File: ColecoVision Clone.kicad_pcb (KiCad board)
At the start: 2 copper layers, 149.4 x 99.1 mm, 141 parts, among them J1 Cartridge Slot, J2 Composite video, J3 PJ-102A, J4 RCJ-017, J5 Controller Port 1, J6 Controller Port 2, Q1 2n4401, Q2 Q_NJFET_DGS, Q3 2N3904, Q4 2N3904, Q5 2N3904, SW1 Power Toggle, SW2 Reset, U1 Z80CPU, U10 SN76489AN, U12 74LS138 (Mem. Mapped), U13 74LS138 (I/O), U14 74LS02, U15 Controller 1, U16 Controller 2, U17 74LS05, U18 74LS05, U19 74HC04, U2 Work RAM, U20 74LS74, U21 74HC04, U22 74LS74, U23 74HCT00, U24 TPS60403DBVR, U3 BIOS ROM 27C256, U4 74HCT04, U5 TMS9918A, U6 74LS574, U7 74LS574, U8 74LS574, U9 VRAM, X1 14.31818MHz

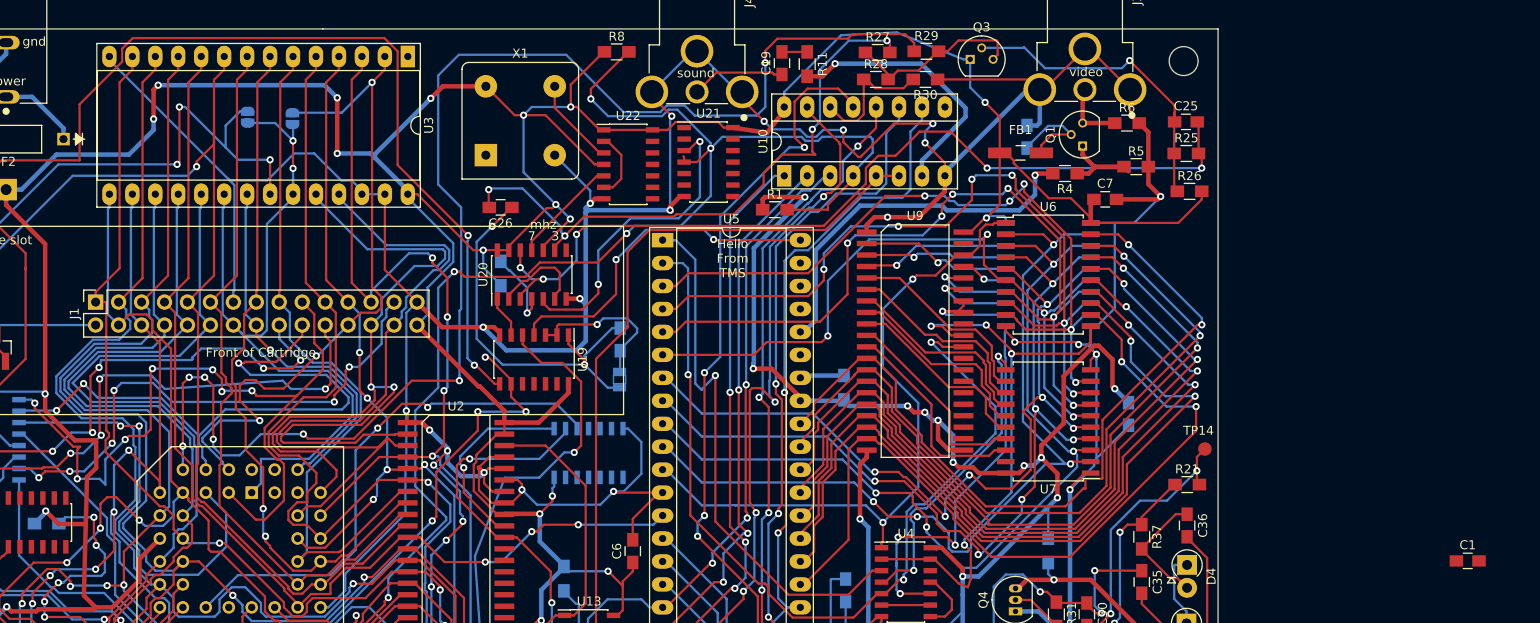
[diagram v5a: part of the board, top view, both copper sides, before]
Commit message: BIOS ROM decouple
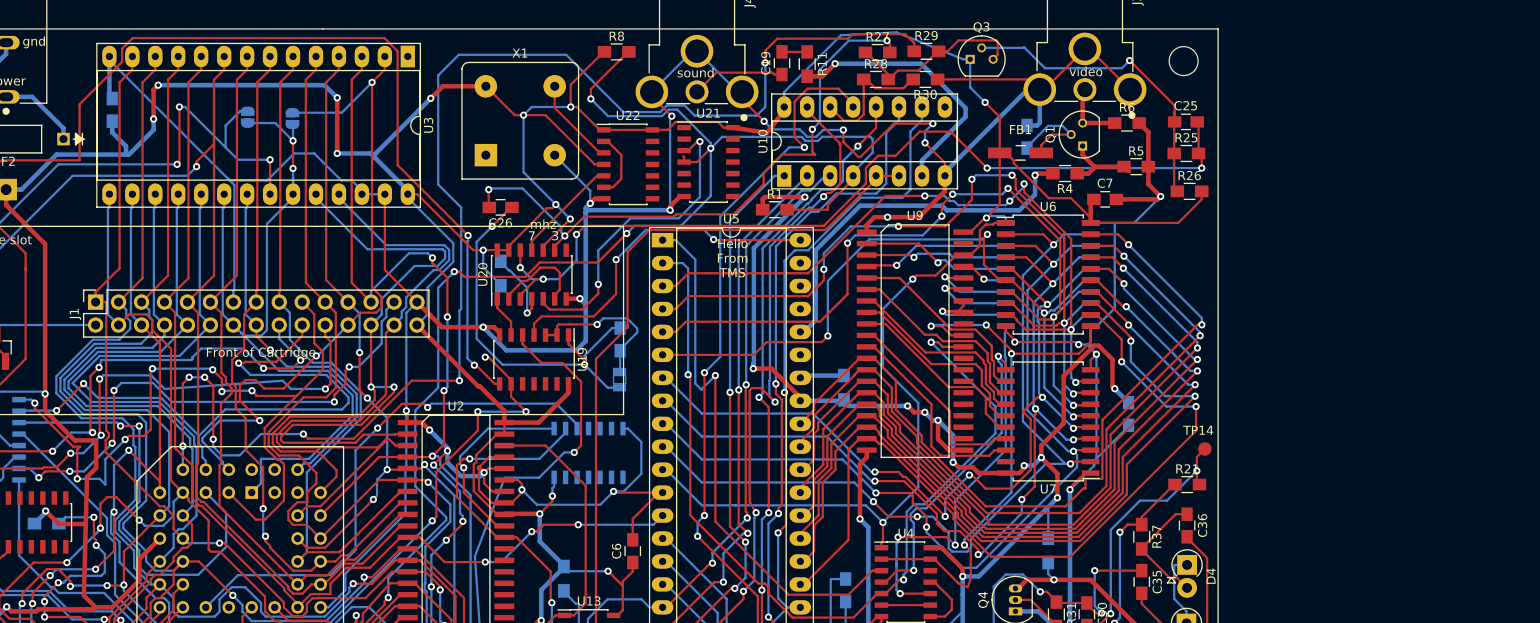
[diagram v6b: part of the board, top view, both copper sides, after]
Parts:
- C1: moved to B.Cu
- moved C1 158.1 mm to (-48.7, 36.9), turned to 90 degrees
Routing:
- net GND: track 871.5 -> 876.3 mm
- net VCC: track 839.4 -> 843.8 mm
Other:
- board text added: ""grime pilot""
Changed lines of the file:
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@@
   (general
     (thickness 1.6)
-    (drawings 27)
-    (tracks 4469)
+    (drawings 28)
+    (tracks 4475)
     (zones 0)
     (modules 141)
@@
     )
   )
-  (module Capacitors_SMD:C_0805_HandSoldering (layer F.Cu)
-    (at 101.2825 86.8045)
+  (module Capacitors_SMD:C_0805_HandSoldering (layer B.Cu)
+    (at -48.7045 36.8935 90)
     (descr "Capacitor SMD 0805, hand soldering")
     (tags "capacitor 0805")
     (attr smd)
-    (fp_text reference C1 (at 0 -1.75) (layer F.SilkS)
-      (effects (font (size 1 1) (thickness 0.15)))
+    (fp_text reference C1 (at 0 1.75 -90) (layer B.SilkS)
+      (effects (font (size 1 1) (thickness 0.15)) (justify mirror))
     )
-    (fp_text value 0.1µF (at 0 1.75) (layer F.Fab)
-      (effects (font (size 1 1) (thickness 0.15)))
+    (fp_text value 0.1µF (at 0 -1.75 -90) (layer B.Fab)
+      (effects (font (size 1 1) (thickness 0.15)) (justify mirror))
     )
-    (fp_text user %R (at 0 -1.75) (layer F.Fab)
-      (effects (font (size 1 1) (thickness 0.15)))
+    (fp_text user %R (at 0 1.75 -90) (layer B.Fab)
+      (effects (font (size 1 1) (thickness 0.15)) (justify mirror))
     )
-    (fp_line (start -1 0.62) (end -1 -0.62) (layer F.Fab) (width 0.1))
-    (fp_line (start 1 0.62) (end -1 0.62) (layer F.Fab) (width 0.1))
-    (fp_line (start 1 -0.62) (end 1 0.62) (layer F.Fab) (width 0.1))
-    (fp_line (start -1 -0.62) (end 1 -0.62) (layer F.Fab) (width 0.1))
-    (fp_line (start 0.5 -0.85) (end -0.5 -0.85) (layer F.SilkS) (width 0.12))
-    (fp_line (start -0.5 0.85) (end 0.5 0.85) (layer F.SilkS) (width 0.12))
-    (fp_line (start -2.25 -0.88) (end 2.25 -0.88) (layer F.CrtYd) (width 0.05))
-    (fp_line (start -2.25 -0.88) (end -2.25 0.87) (layer F.CrtYd) (width 0.05))
-    (fp_line (start 2.25 0.87) (end 2.25 -0.88) (layer F.CrtYd) (width 0.05))
-    (fp_line (start 2.25 0.87) (end -2.25 0.87) (layer F.CrtYd) (width 0.05))
-    (pad 1 smd rect (at -1.25 0) (size 1.5 1.25) (layers F.Cu F.Paste F.Mask)
+    (fp_line (start -1 -0.62) (end -1 0.62) (layer B.Fab) (width 0.1))
+    (fp_line (start 1 -0.62) (end -1 -0.62) (layer B.Fab) (width 0.1))
+    (fp_line (start 1 0.62) (end 1 -0.62) (layer B.Fab) (width 0.1))
+    (fp_line (start -1 0.62) (end 1 0.62) (layer B.Fab) (width 0.1))
+    (fp_line (start 0.5 0.85) (end -0.5 0.85) (layer B.SilkS) (width 0.12))
+    (fp_line (start -0.5 -0.85) (end 0.5 -0.85) (layer B.SilkS) (width 0.12))
+    (fp_line (start -2.25 0.88) (end 2.25 0.88) (layer B.CrtYd) (width 0.05))
+    (fp_line (start -2.25 0.88) (end -2.25 -0.87) (layer B.CrtYd) (width 0.05))
+    (fp_line (start 2.25 -0.87) (end 2.25 0.88) (layer B.CrtYd) (width 0.05))
+    (fp_line (start 2.25 -0.87) (end -2.25 -0.87) (layer B.CrtYd) (width 0.05))
+    (pad 1 smd rect (at -1.25 0 90) (size 1.5 1.25) (layers B.Cu B.Paste B.Mask)
       (net 19 VCC))
-    (pad 2 smd rect (at 1.25 0) (size 1.5 1.25) (layers F.Cu F.Paste F.Mask)
+    (pad 2 smd rect (at 1.25 0 90) (size 1.5 1.25) (layers B.Cu B.Paste B.Mask)
       (net 10 GND))
     (model Capacitors_SMD.3dshapes/C_0805.wrl
@@
       (xy -3.70249 -1.164682) (xy -3.429 -1.183342) (xy -2.925182 -1.118187)) (layer F.SilkS) (width 0.01))
   )
+  (gr_text "\"grime pilot\"" (at -62.5475 124.968) (layer B.SilkS)
+    (effects (font (size 1 1) (thickness 0.15)) (justify mirror))
+  )
   (gr_text power (at -60.3885 33.7185) (layer F.SilkS)
     (effects (font (size 1 1) (thickness 0.15)))
@@
   (segment (start 66.9925 46.7995) (end 67.31 46.482) (width 0.5) (layer F.Cu) (net 10))
   (segment (start 62.4205 46.7995) (end 66.9925 46.7995) (width 0.5) (layer F.Cu) (net 10))
+  (segment (start -49.022 35.326) (end -48.7045 35.6435) (width 0.5) (layer B.Cu) (net 10))
+  (segment (start -49.022 30.988) (end -49.022 35.326) (width 0.5) (layer B.Cu) (net 10))
   (segment (start 7.214 92.837) (end 7.7855 92.2655) (width 0.25) (layer F.Cu) (net 19) (status 10))
   (segment (start 6.764 92.837) (end 7.214 92.837) (width 0.25) (layer F.Cu) (net 19) (status 30))
@@
   (segment (start -58.752 45.72) (end -54.8785 41.8465) (width 0.5) (layer B.Cu) (net 19))
   (segment (start -60.452 45.72) (end -58.752 45.72) (width 0.5) (layer B.Cu) (net 19) (status 10))
-  (segment (start -54.8785 41.8465) (end -46.863 41.8465) (width 0.5) (layer B.Cu) (net 19))
   (segment (start -46.863 41.8465) (end -44.1325 39.116) (width 0.5) (layer B.Cu) (net 19))
   (segment (start -44.1325 39.116) (end -44.1325 37.9095) (width 0.5) (layer B.Cu) (net 19))
@@
   (segment (start 59.564 47.156) (end 59.9205 46.7995) (width 0.5) (layer F.Cu) (net 19))
   (segment (start 59.564 49.403) (end 59.564 47.156) (width 0.5) (layer F.Cu) (net 19))
+  (segment (start -48.7045 39.3935) (end -47.1805 40.9175) (width 0.5) (layer B.Cu) (net 19))
+  (segment (start -48.7045 38.1435) (end -48.7045 39.3935) (width 0.5) (layer B.Cu) (net 19))
+  (segment (start -47.1805 41.8465) (end -46.863 41.8465) (width 0.5) (layer B.Cu) (net 19))
+  (segment (start -47.1805 40.9175) (end -47.1805 41.8465) (width 0.5) (layer B.Cu) (net 19))
+  (segment (start -54.8785 41.8465) (end -47.1805 41.8465) (width 0.5) (layer B.Cu) (net 19))
   (via (at 53.407809 44.12749) (size 0.8) (drill 0.4) (layers F.Cu B.Cu) (net 20))
   (segment (start 53.407809 46.274879) (end 53.407809 44.693175) (width 0.5) (layer B.Cu) (net 20))

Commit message: SO CLOSE
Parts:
- C10, C11, C14, C16, C18, C29: moved to B.Cu
- moved C17 321.2 mm to (-64.3, 75.7), turned to 270 degrees
- moved C15 283.2 mm to (-52.2, 52.4), turned to 90 degrees
- moved C18 272.9 mm to (-32.7, 86.6)
- moved C14 261.9 mm to (-10.3, 72.0), turned to 270 degrees
- moved C2 254.4 mm to (-11.3, 38.4), turned to 270 degrees
- moved C16 252.7 mm to (4.00, 85.2)
- moved C29 243.9 mm to (-3.22, 39.9)
- moved C9 100.9 mm to (67.5, 54.8), turned to 270 degrees
- moved C11 90.9 mm to (39.9, 73.7), turned to 180 degrees
- moved C10 90.4 mm to (40.4, 65.6)
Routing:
- net GND: track 876.3 -> 1006.4 mm, vias 48 -> 57
- net VCC: track 843.8 -> 906.4 mm, vias 43 -> 46
- net A4: track 79.7 -> 84.7 mm
- net RW: track 75.1 -> 78.1 mm
- net D7: track 296.9 -> 299.3 mm
- net VD6: track 86.6 -> 85.2 mm
- net AD7: track 82.7 -> 83.8 mm
- net D3: track 268.0 -> 267.4 mm

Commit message: 3
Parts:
- C28: moved to B.Cu
- moved C28 236.2 mm to (8.51, 43.1), turned to 270 degrees
- moved C13 227.1 mm to (46.4, 37.2), turned to 270 degrees
- moved C22 183.6 mm to (50.9, 97.0)
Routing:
- net GND: track 1006.4 -> 1021.3 mm
- net VCC: track 906.4 -> 915.8 mm, vias 46 -> 47
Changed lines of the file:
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@@
     (thickness 1.6)
     (drawings 28)
-    (tracks 4619)
+    (tracks 4632)
     (zones 0)
     (modules 141)
@@
     )
   )
-  (module Capacitors_SMD:C_0805_HandSoldering (layer F.Cu)
-    (at 223.608 140.692)
+  (module Capacitors_SMD:C_0805_HandSoldering (layer B.Cu)
+    (at 8.509 43.053 270)
     (descr "Capacitor SMD 0805, hand soldering")
     (tags "capacitor 0805")
     (attr smd)
-    (fp_text reference C28 (at 0 -1.75) (layer F.SilkS)
-      (effects (font (size 1 1) (thickness 0.15)))
+    (fp_text reference C28 (at 0 1.75 270) (layer B.SilkS)
+      (effects (font (size 1 1) (thickness 0.15)) (justify mirror))
     )
-    (fp_text value 0.1µF (at 0 1.75) (layer F.Fab)
-      (effects (font (size 1 1) (thickness 0.15)))
+    (fp_text value 0.1µF (at 0 -1.75 270) (layer B.Fab)
+      (effects (font (size 1 1) (thickness 0.15)) (justify mirror))
     )
-    (fp_text user %R (at 0 -1.75) (layer F.Fab)
-      (effects (font (size 1 1) (thickness 0.15)))
+    (fp_text user %R (at 0 1.75 270) (layer B.Fab)
+      (effects (font (size 1 1) (thickness 0.15)) (justify mirror))
     )
-    (fp_line (start -1 0.62) (end -1 -0.62) (layer F.Fab) (width 0.1))
-    (fp_line (start 1 0.62) (end -1 0.62) (layer F.Fab) (width 0.1))
-    (fp_line (start 1 -0.62) (end 1 0.62) (layer F.Fab) (width 0.1))
-    (fp_line (start -1 -0.62) (end 1 -0.62) (layer F.Fab) (width 0.1))
-    (fp_line (start 0.5 -0.85) (end -0.5 -0.85) (layer F.SilkS) (width 0.12))
-    (fp_line (start -0.5 0.85) (end 0.5 0.85) (layer F.SilkS) (width 0.12))
-    (fp_line (start -2.25 -0.88) (end 2.25 -0.88) (layer F.CrtYd) (width 0.05))
-    (fp_line (start -2.25 -0.88) (end -2.25 0.87) (layer F.CrtYd) (width 0.05))
-    (fp_line (start 2.25 0.87) (end 2.25 -0.88) (layer F.CrtYd) (width 0.05))
-    (fp_line (start 2.25 0.87) (end -2.25 0.87) (layer F.CrtYd) (width 0.05))
-    (pad 1 smd rect (at -1.25 0) (size 1.5 1.25) (layers F.Cu F.Paste F.Mask)
+    (fp_line (start -1 -0.62) (end -1 0.62) (layer B.Fab) (width 0.1))
+    (fp_line (start 1 -0.62) (end -1 -0.62) (layer B.Fab) (width 0.1))
+    (fp_line (start 1 0.62) (end 1 -0.62) (layer B.Fab) (width 0.1))
+    (fp_line (start -1 0.62) (end 1 0.62) (layer B.Fab) (width 0.1))
+    (fp_line (start 0.5 0.85) (end -0.5 0.85) (layer B.SilkS) (width 0.12))
+    (fp_line (start -0.5 -0.85) (end 0.5 -0.85) (layer B.SilkS) (width 0.12))
+    (fp_line (start -2.25 0.88) (end 2.25 0.88) (layer B.CrtYd) (width 0.05))
+    (fp_line (start -2.25 0.88) (end -2.25 -0.87) (layer B.CrtYd) (width 0.05))
+    (fp_line (start 2.25 -0.87) (end 2.25 0.88) (layer B.CrtYd) (width 0.05))
+    (fp_line (start 2.25 -0.87) (end -2.25 -0.87) (layer B.CrtYd) (width 0.05))
+    (pad 1 smd rect (at -1.25 0 270) (size 1.5 1.25) (layers B.Cu B.Paste B.Mask)
       (net 19 VCC))
-    (pad 2 smd rect (at 1.25 0) (size 1.5 1.25) (layers F.Cu F.Paste F.Mask)
+    (pad 2 smd rect (at 1.25 0 270) (size 1.5 1.25) (layers B.Cu B.Paste B.Mask)
       (net 10 GND))
     (model Capacitors_SMD.3dshapes/C_0805.wrl
@@
   )
   (module Capacitors_SMD:C_0805_HandSoldering (layer F.Cu)
-    (at 228.548 143.512)
+    (at 50.947 96.9645)
     (descr "Capacitor SMD 0805, hand soldering")
     (tags "capacitor 0805")
@@
   )
   (module Capacitors_SMD:C_0805_HandSoldering (layer F.Cu)
-    (at 253.988 129.272)
+    (at 46.4185 37.1675 270)
     (descr "Capacitor SMD 0805, hand soldering")
     (tags "capacitor 0805")
     (attr smd)
-    (fp_text reference C13 (at 0 -1.75) (layer F.SilkS)
+    (fp_text reference C13 (at 0 -1.75 90) (layer F.SilkS)
       (effects (font (size 1 1) (thickness 0.15)))
     )
-    (fp_text value 0.1µF (at 0 1.75) (layer F.Fab)
+    (fp_text value 0.1µF (at 0 1.75 90) (layer F.Fab)
       (effects (font (size 1 1) (thickness 0.15)))
     )
-    (fp_text user %R (at 0 -1.75) (layer F.Fab)
+    (fp_text user %R (at 0 -1.75 90) (layer F.Fab)
       (effects (font (size 1 1) (thickness 0.15)))
     )
@@
     (fp_line (start 2.25 0.87) (end 2.25 -0.88) (layer F.CrtYd) (width 0.05))
     (fp_line (start 2.25 0.87) (end -2.25 0.87) (layer F.CrtYd) (width 0.05))
-    (pad 1 smd rect (at -1.25 0) (size 1.5 1.25) (layers F.Cu F.Paste F.Mask)
+    (pad 1 smd rect (at -1.25 0 270) (size 1.5 1.25) (layers F.Cu F.Paste F.Mask)
       (net 19 VCC))
-    (pad 2 smd rect (at 1.25 0) (size 1.5 1.25) (layers F.Cu F.Paste F.Mask)
+    (pad 2 smd rect (at 1.25 0 270) (size 1.5 1.25) (layers F.Cu F.Paste F.Mask)
       (net 10 GND))
     (model Capacitors_SMD.3dshapes/C_0805.wrl
@@
   (segment (start 1.981 48.971) (end 2.032 48.92) (width 0.25) (layer F.Cu) (net 19))
   (via (at 1.981 48.971) (size 0.8) (drill 0.4) (layers F.Cu B.Cu) (net 19))
-  (segment (start 4.682 42.926) (end -0.762 37.482) (width 0.25) (layer F.Cu) (net 19))
+  (segment (start 4.682 42.926) (end 3.9285 42.1725) (width 0.25) (layer F.Cu) (net 19))
   (segment (start 5.682 42.926) (end 4.682 42.926) (width 0.25) (layer F.Cu) (net 19) (status 10))
   (segment (start -4.174 37.482) (end -7.366 34.29) (width 0.25) (layer F.Cu) (net 19) (status 20))
@@
   (segment (start -32.893 85.217) (end -31.496 86.614) (width 0.5) (layer B.Cu) (net 10))
   (segment (start -32.893 83.312) (end -32.893 85.217) (width 0.5) (layer B.Cu) (net 10))
+  (segment (start 46.4185 38.4175) (end 42.1005 38.4175) (width 0.5) (layer F.Cu) (net 10))
+  (segment (start 52.197 93.345) (end 51.2445 92.3925) (width 0.5) (layer F.Cu) (net 10))
+  (segment (start 52.197 96.9645) (end 52.197 93.345) (width 0.5) (layer F.Cu) (net 10))
+  (segment (start 7.132 44.303) (end 4.191 47.244) (width 0.5) (layer B.Cu) (net 10))
+  (segment (start 8.509 44.303) (end 7.132 44.303) (width 0.5) (layer B.Cu) (net 10))
   (segment (start 7.214 92.837) (end 7.7855 92.2655) (width 0.25) (layer F.Cu) (net 19) (status 10))
   (segment (start 6.764 92.837) (end 7.214 92.837) (width 0.25) (layer F.Cu) (net 19) (status 30))
@@
   (segment (start -42.550501 85.211499) (end -43.434 84.328) (width 0.5) (layer B.Cu) (net 19))
   (segment (start -42.550501 85.719499) (end -42.550501 85.211499) (width 0.5) (layer B.Cu) (net 19))
+  (segment (start 46.569 36.068) (end 46.4185 35.9175) (width 0.5) (layer F.Cu) (net 19))
+  (segment (start 47.879 36.068) (end 46.569 36.068) (width 0.5) (layer F.Cu) (net 19))
+  (segment (start 49.697 98.3215) (end 48.4505 99.568) (width 0.5) (layer F.Cu) (net 19))
+  (segment (start 49.697 96.9645) (end 49.697 98.3215) (width 0.5) (layer F.Cu) (net 19))
+  (segment (start 3.9285 42.1725) (end -0.762 37.482) (width 0.25) (layer F.Cu) (net 19))
+  (via (at 3.9285 42.1725) (size 0.8) (drill 0.4) (layers F.Cu B.Cu) (net 19))
+  (segment (start 4.298 41.803) (end 3.9285 42.1725) (width 0.5) (layer B.Cu) (net 19))
+  (segment (start 8.509 41.803) (end 4.298 41.803) (width 0.5) (layer B.Cu) (net 19))
   (via (at 53.407809 44.12749) (size 0.8) (drill 0.4) (layers F.Cu B.Cu) (net 20))
   (segment (start 53.407809 46.274879) (end 53.407809 44.693175) (width 0.5) (layer B.Cu) (net 20))
